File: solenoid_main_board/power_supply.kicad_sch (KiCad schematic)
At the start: 8 parts, among them U3 LM78M05

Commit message: main board layout
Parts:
- C7: footprint Capacitor_SMD:C_1206_3216Metric_Pad1.33x1.80mm_HandSolder -> Capacitor_SMD:C_0603_1608Metric_Pad1.08x0.95mm_HandSolder
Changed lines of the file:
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@@
 			)
 		)
-		(property "Footprint" "Capacitor_SMD:C_1206_3216Metric_Pad1.33x1.80mm_HandSolder"
+		(property "Footprint" "Capacitor_SMD:C_0603_1608Metric_Pad1.08x0.95mm_HandSolder"
 			(at 89.8652 80.01 0)
 			(effects

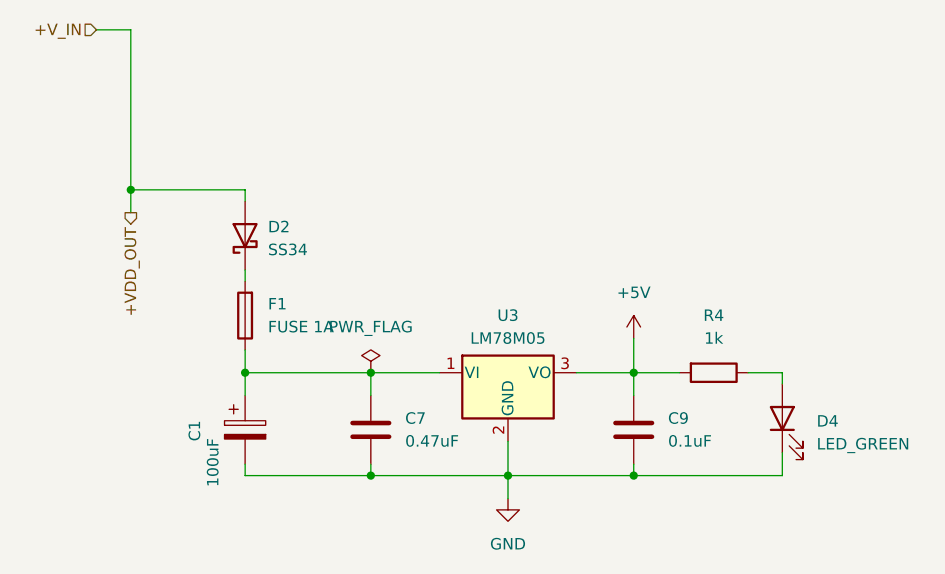
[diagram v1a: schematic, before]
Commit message: Solenoid main board finished
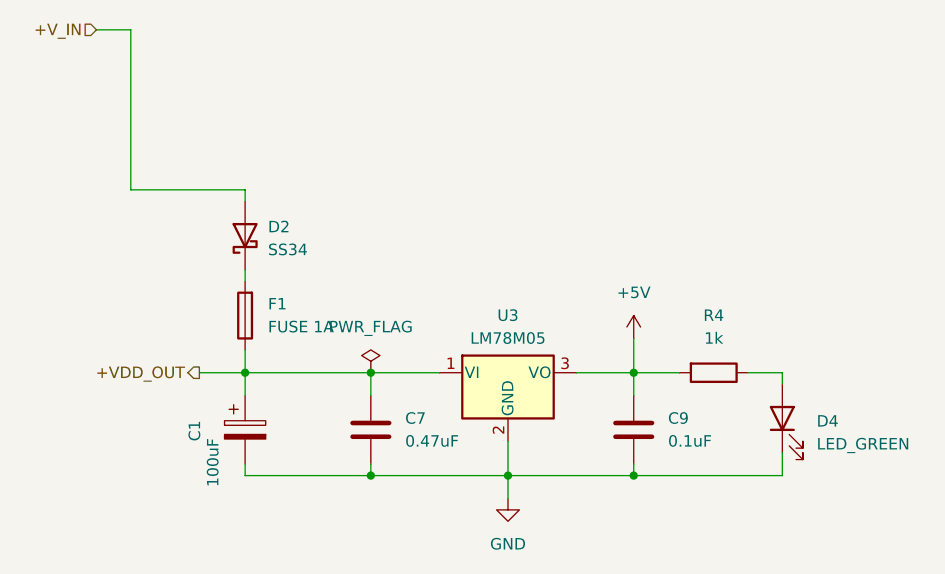
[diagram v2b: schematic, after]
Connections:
- net +VDD_OUT: now also C1.1, C7.1, F1.1, U3.1 (VI); no longer D2.2 (A)
- new net +V_IN: D2.2 (A)
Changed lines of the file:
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@@
-	)
-	(junction
-		(at 62.23 49.53)
-		(diameter 0)
-		(color 0 0 0 0)
 	)
 	(junction
@@
 	(wire
 		(pts
+			(xy 69.85 69.85) (xy 74.93 69.85)
+		)
+		(stroke
+			(width 0)
+			(type default)
+		)
+	)
+	(wire
+		(pts
 			(xy 74.93 72.39) (xy 74.93 69.85)
 		)
@@
 		(pts
 			(xy 96.52 69.85) (xy 88.9 69.85)
-		)
-		(stroke
-			(width 0)
-			(type default)
-		)
-	)
-	(wire
-		(pts
-			(xy 62.23 49.53) (xy 62.23 52.07)
 		)
 		(stroke
@@
 	(hierarchical_label "+VDD_OUT"
 		(shape output)
-		(at 62.23 52.07 270)
+		(at 69.85 69.85 180)
 		(effects
 			(font
